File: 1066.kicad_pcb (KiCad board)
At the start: 2 copper layers, 228.6 x 139.7 mm, 83 parts, among them J1 Conn_01x03, P1 Conn_01x50_Male_Atari_1066, P2 Conn_01x40_Male, SW1 Bank, U1 74LS156, U10 4164, U11 4164, U12 74LS157, U13 74LS257, U14 74LS257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

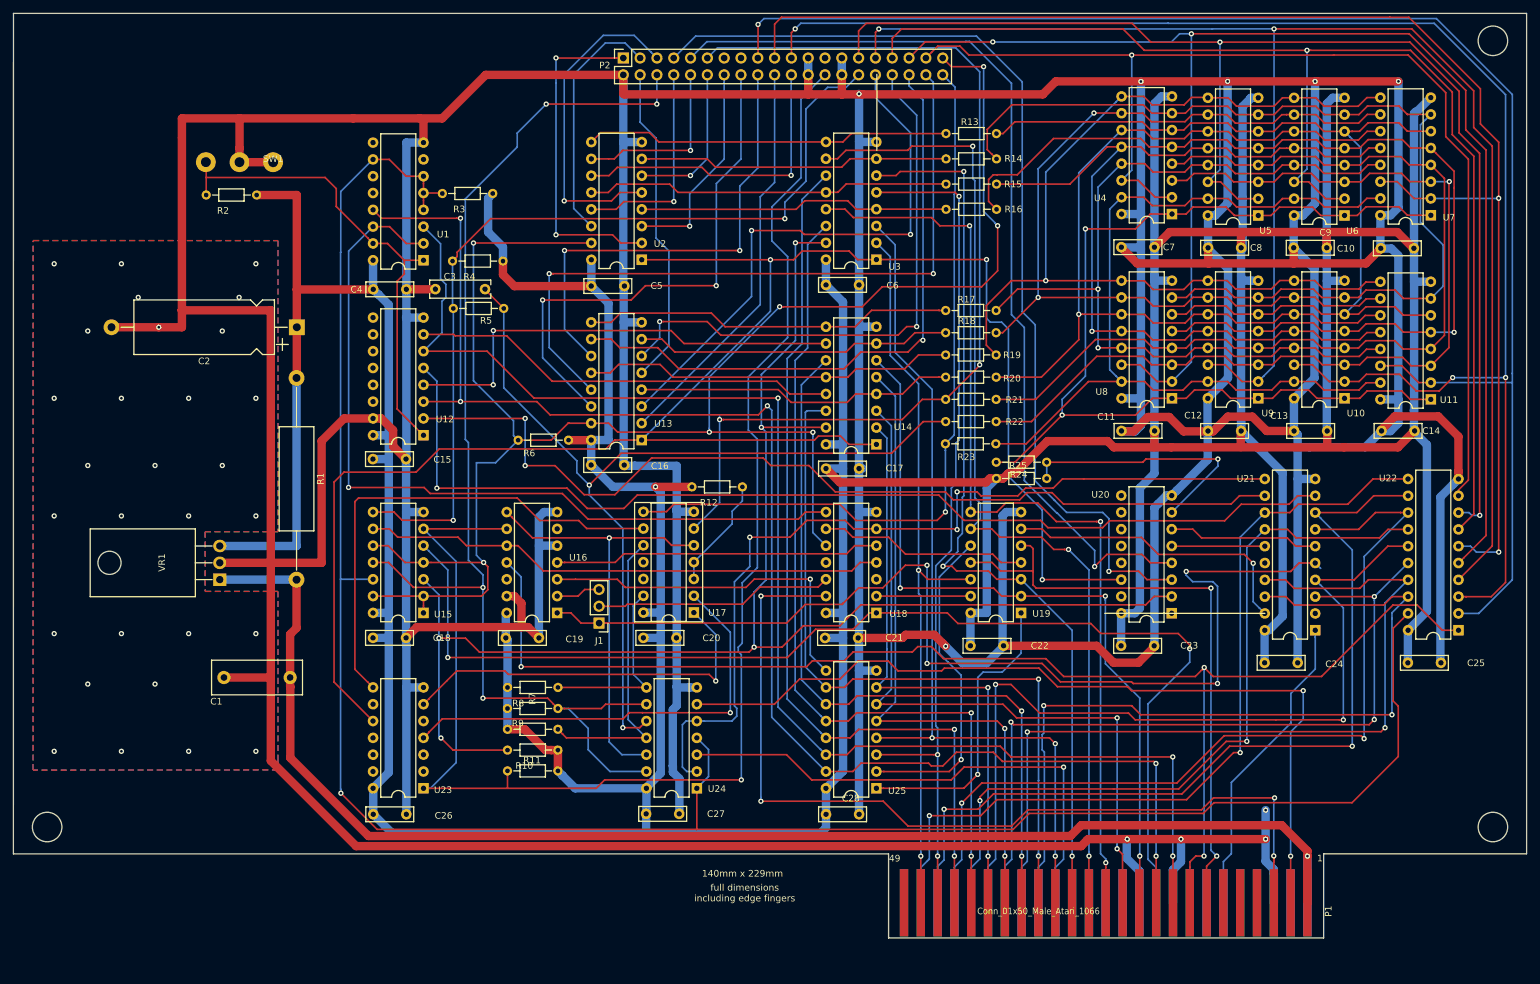
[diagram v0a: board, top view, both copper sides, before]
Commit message: apply fixes to sw1 c1 j1 and edge connector as pointed out by atari-passion on atariage.com
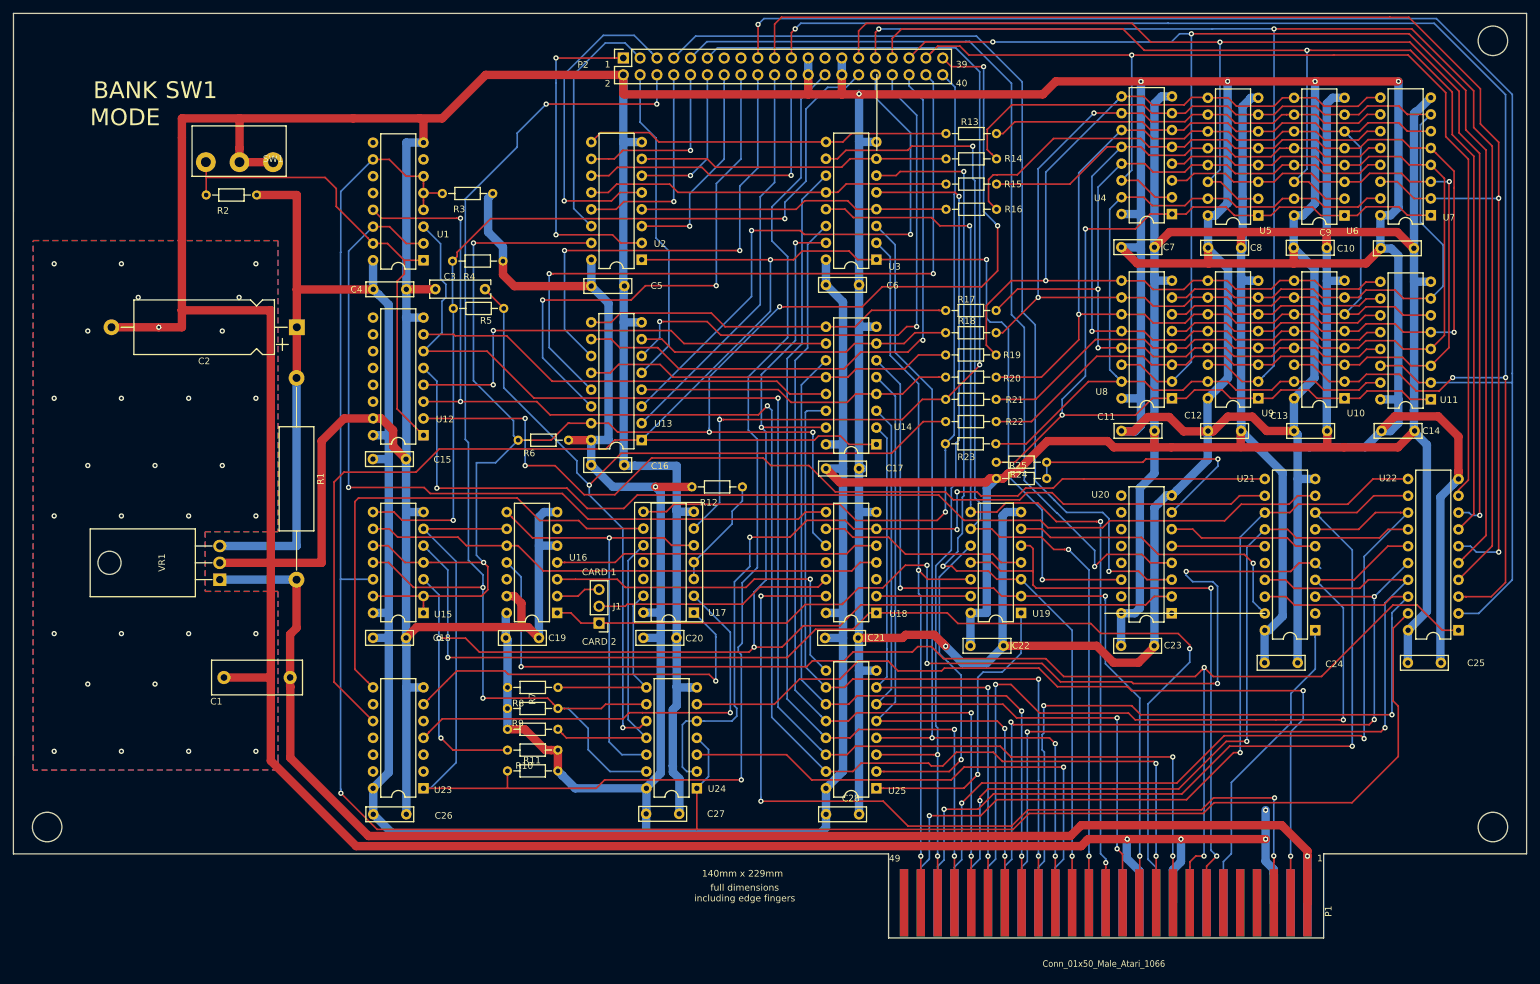
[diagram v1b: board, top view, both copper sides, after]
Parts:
- C1: value .1uF -> .22uF
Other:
- board text added: "39"
- board text added: "40"
- board text added: "BANK MODE"
- board text added: "CARD 1"
- board text added: "CARD 2"
- board text added: "SW1"
